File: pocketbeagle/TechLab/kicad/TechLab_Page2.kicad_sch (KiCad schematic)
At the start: 47 parts, among them T1 EAALSTIC1708A0, T2 3904, U5 MCP23S18-E/MJ, U6 FT230XQ-R, X2 10118192-0001LF

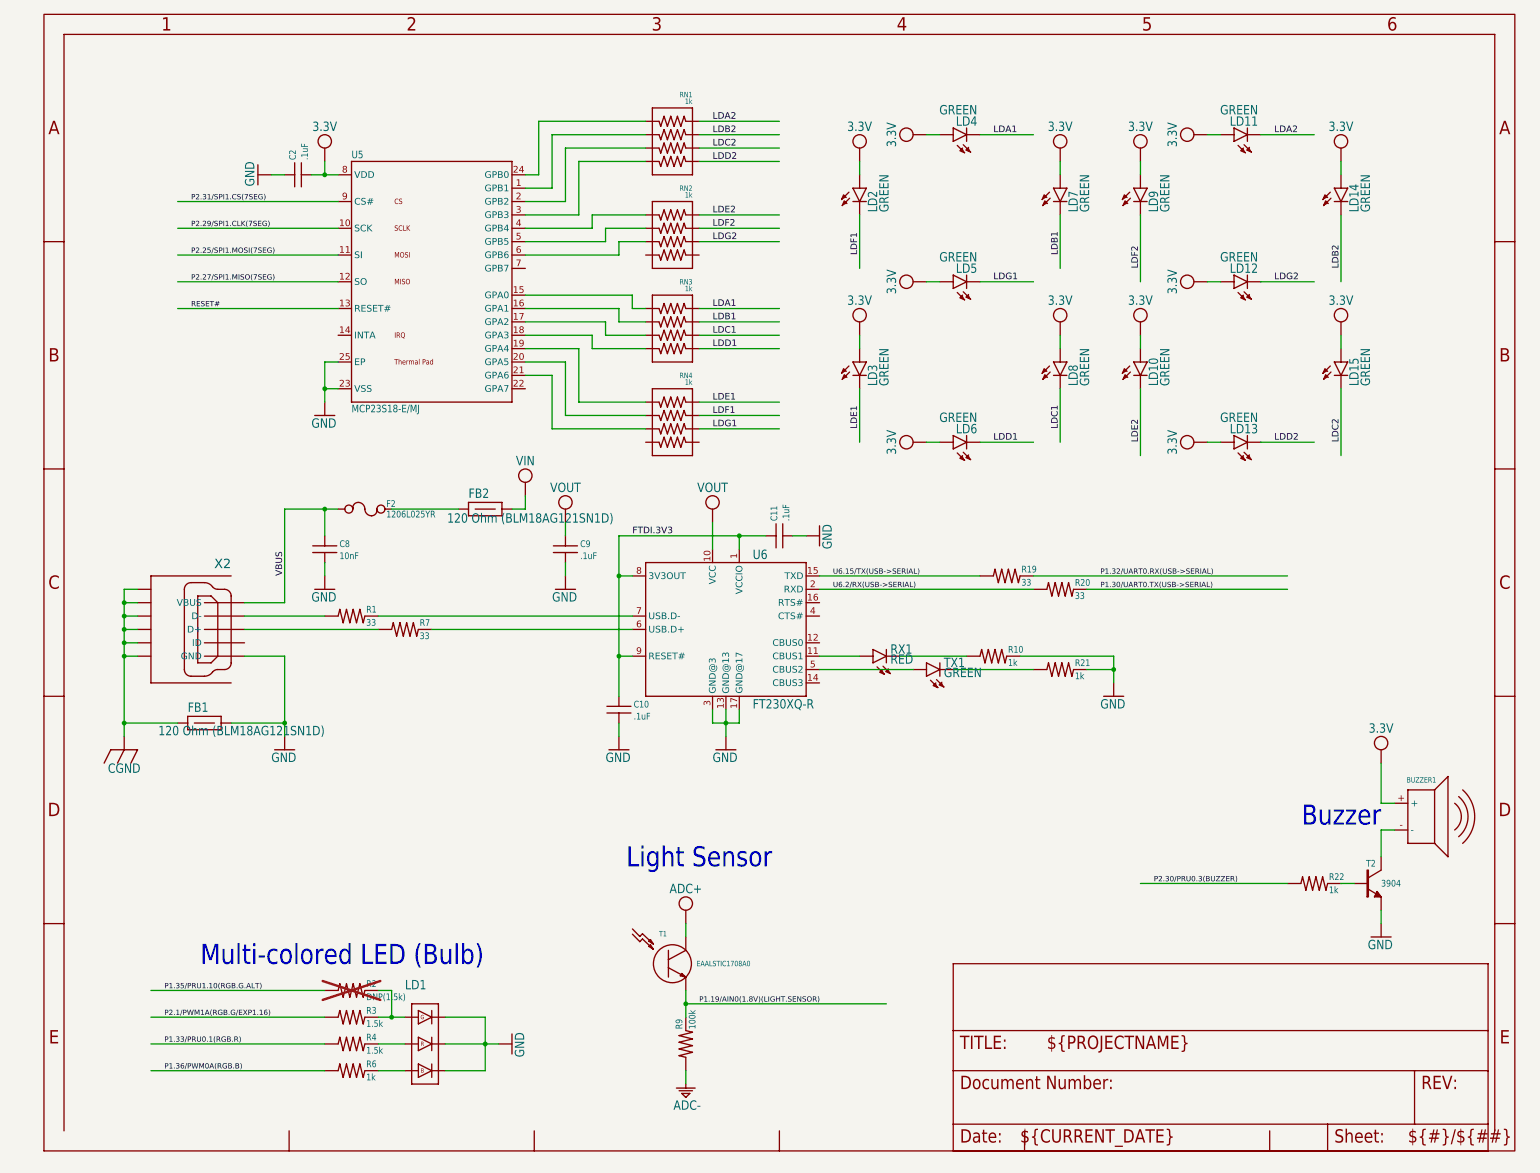
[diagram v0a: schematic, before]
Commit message: TechLab: Update title block for cleaner print
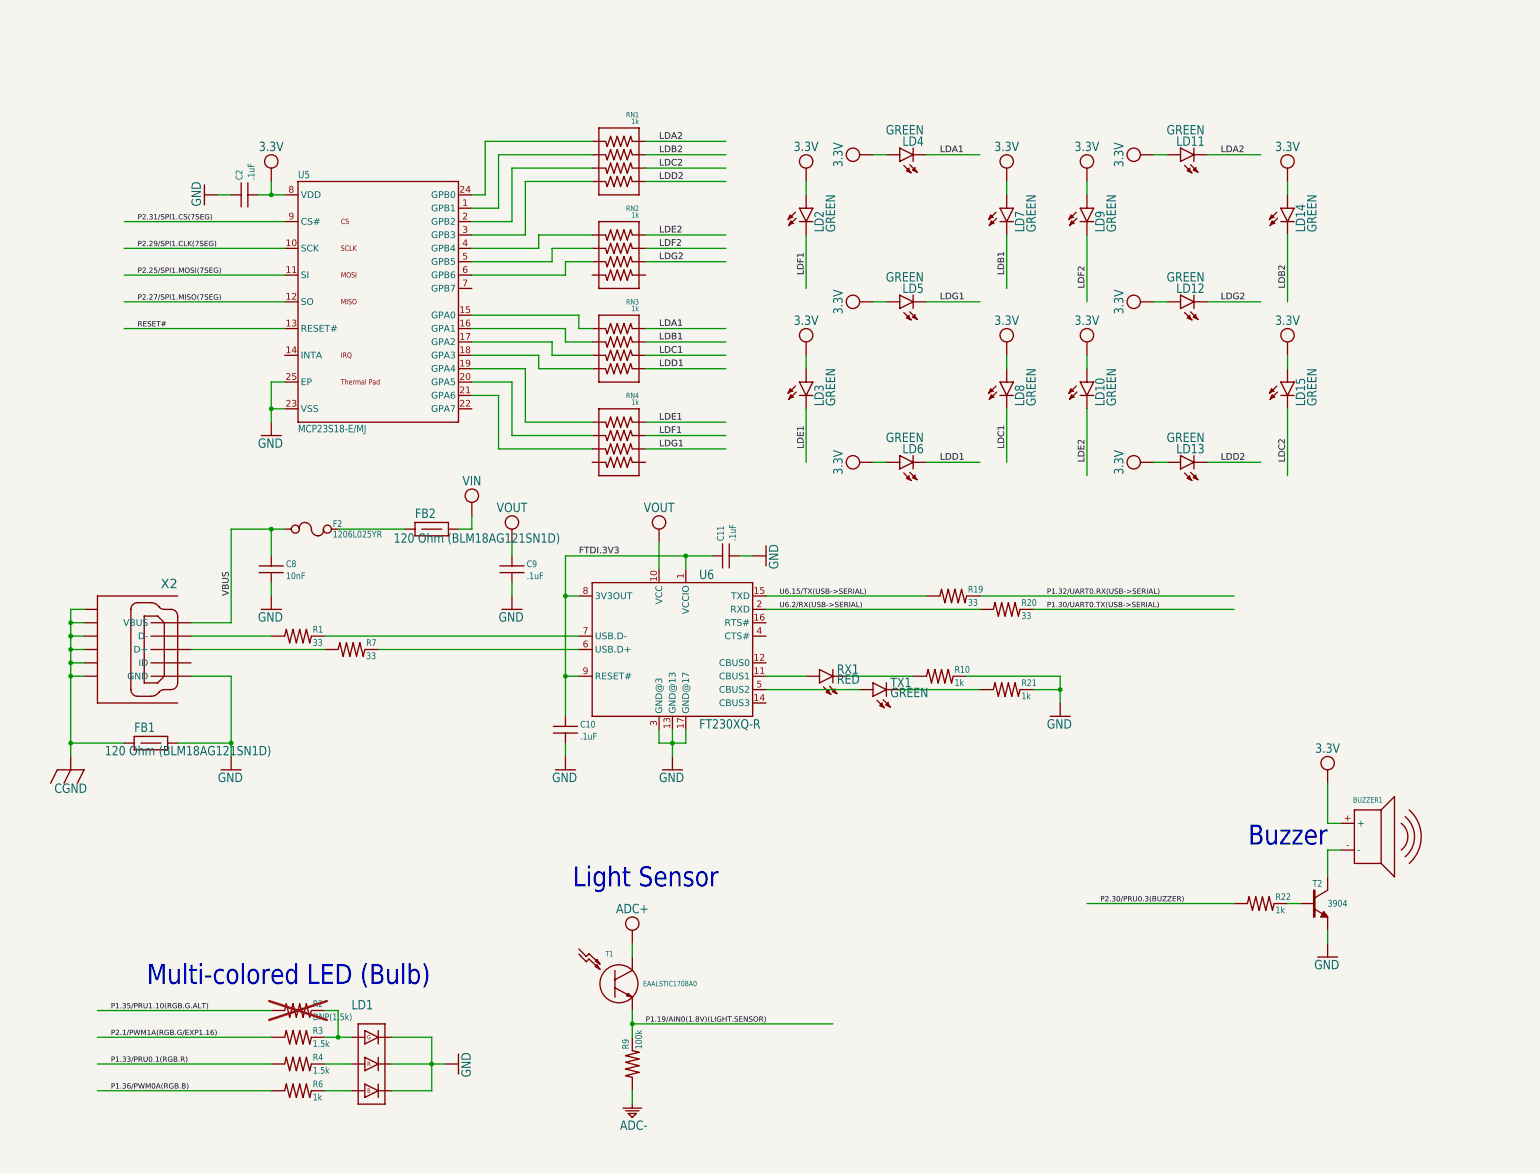
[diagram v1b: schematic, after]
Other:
- company: (none) -> BeagleBoard.org Foundation
- title: (none) -> PocketBeagle TechLab
- moved on the sheet: BUZZER1, C10, C11, C2, C8, C9, F2, FB1, FB2, LD1, LD10, LD11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

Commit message: Add USB C and 3-pin JST SH for UART with analog switch
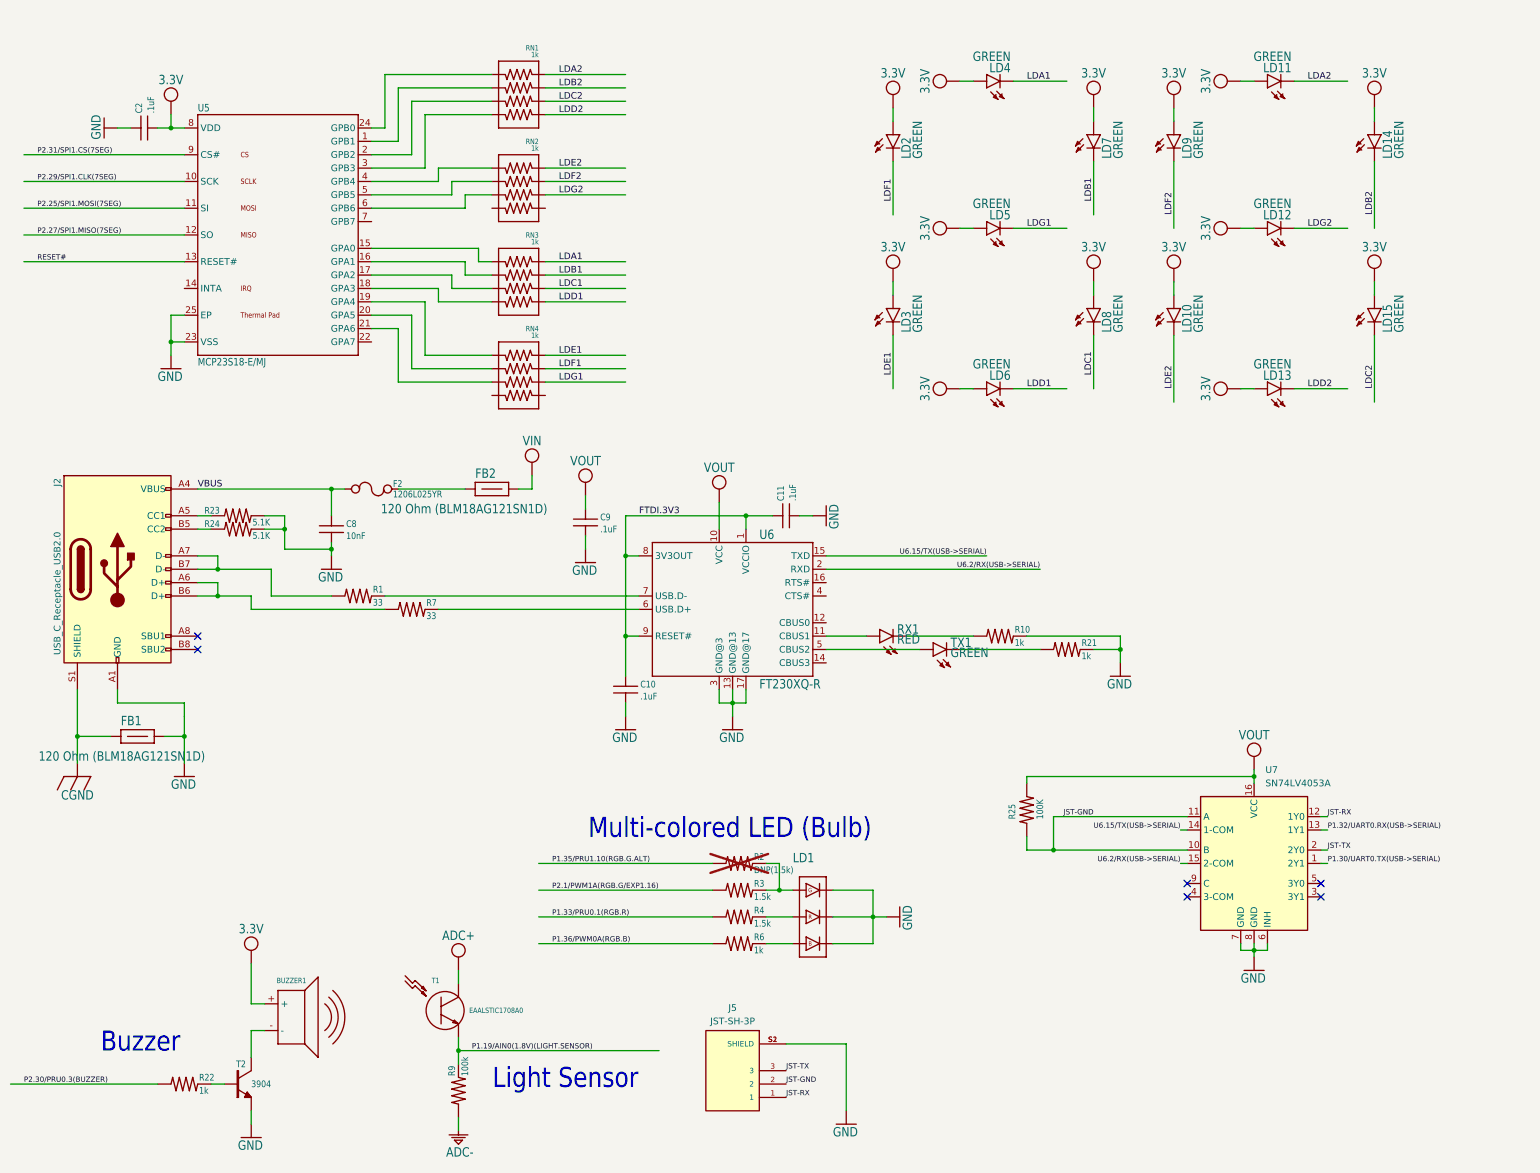
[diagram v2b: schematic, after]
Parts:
- removed R19, R20: 33, TechLab:0402, symbol TechLab-eagle-import:RESISTOR-(INCH)-0402
- removed X2: 10118192-0001LF, TechLab:10118192-0001LF(MICRO-USB-B-AMPHENOL-FCI), symbol TechLab-eagle-import:10118192-0001LF
- added J2: USB_C_Receptacle_USB2.0, Connector_USB:USB_C_Receptacle_GCT_USB4105-xx-A_16P_TopMnt_Horizontal, symbol Connector:USB_C_Receptacle_USB2.0
- added J5: JST-SH-3P, Upside Down Labs:JST-SH-3P, symbol Upside Down Labs:JST-SH-3P
- added R23, R24: 5.1K, Upside Down Labs:0402, symbol TechLab-eagle-import:RESISTOR-(INCH)-0402
- added R25: 100K, Upside Down Labs:0402, symbol TechLab-eagle-import:RESISTOR-(INCH)-0402
- added U7: SN74LV4053A, Upside Down Labs:SOT-23-THN-16, symbol Upside Down Labs:SN74LV4053A
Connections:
- net CGND: now also J2.S1 (SHIELD)
- net GND: now also J2.A1 (GND), J2.A12 (GND), J2.B1 (GND), J2.B12 (GND), J5.S1 (SHIELD), J5.S2 (SHIELD), R23.2, R24.2, U7.6 (INH), U7.7 (GND), U7.8 (GND)
- net P1.30/UART0.TX(USB->SERIAL): now also U7.1 (2Y1)
- net P1.32/UART0.RX(USB->SERIAL): now also U7.13 (1Y1)
- net U6.15/TX(USB->SERIAL): now also U7.14 (1-COM)
- net U6.2/RX(USB->SERIAL): now also U7.15 (2-COM)
- net VBUS: now also J2.A4 (VBUS), J2.A9 (VBUS), J2.B4 (VBUS), J2.B9 (VBUS)
- net VOUT: now also R25.2, U7.16 (VCC)
- net at R7.1: now also J2.A6 (D+), J2.B6 (D+)
- net at R1.1: now also J2.A7 (D-), J2.B7 (D-)
- new net: J2.A5 (CC1), R23.1
- new net: J2.B5 (CC2), R24.1
- new net JST-GND: J5.2, R25.1, U7.10 (B), U7.11 (A)
- new net JST-RX: J5.1, U7.12 (1Y0)
- new net JST-TX: J5.3, U7.2 (2Y0)
- no-connect marks 0 -> 6
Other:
- moved on the sheet: BUZZER1, C10, C11, C2, C8, C9, F2, FB1, FB2, LD1, LD10, LD11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

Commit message: TechLab: back-annotate BOM
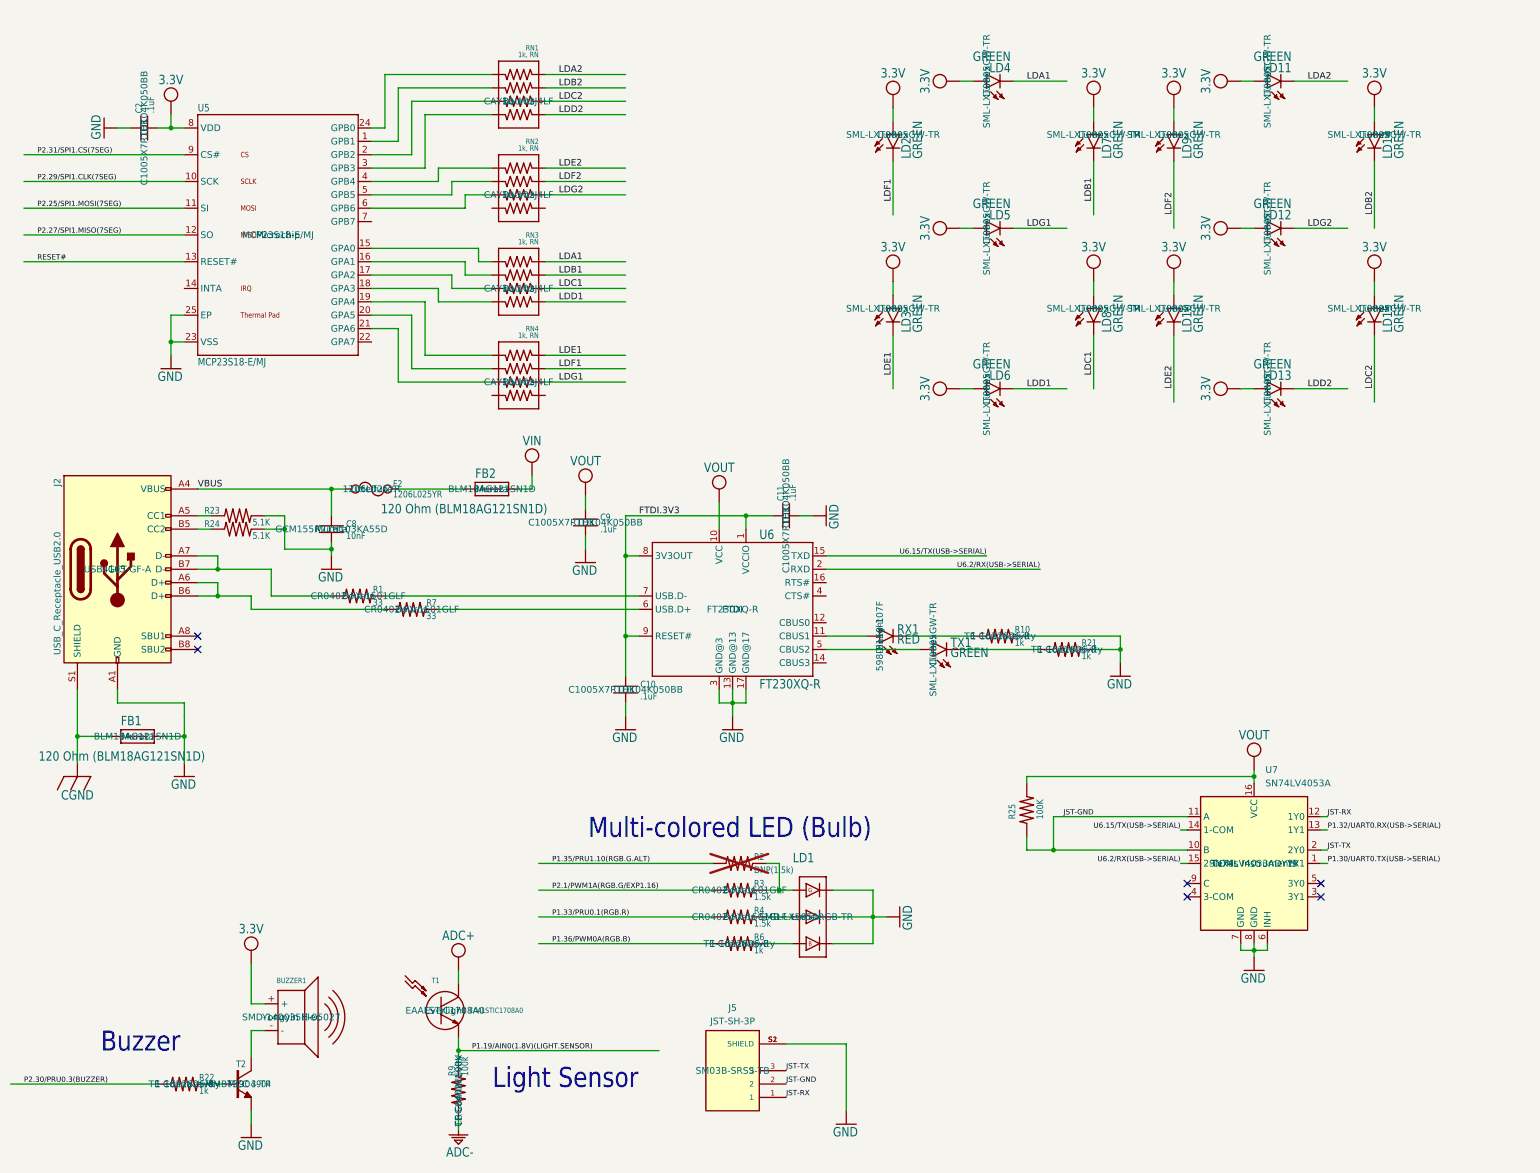
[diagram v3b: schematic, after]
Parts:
- BUZZER1: MANUFACTURER (none) -> Yongyin Elec; MPN (none) -> SMD-140035H-05027
- C10, C11, C2, C9: MANUFACTURER (none) -> TDK; MPN (none) -> C1005X7R1H104K050BB
- C8: MANUFACTURER (none) -> Murata; MPN (none) -> GCM155R71H103KA55D
- F2: MANUFACTURER (none) -> Littelfuse; MPN (none) -> 1206L025YR
- FB1, FB2: MANUFACTURER (none) -> Murata; MPN (none) -> BLM18AG121SN1D
- J2: MANUFACTURER (none) -> GCT; MPN (none) -> USB4105-GF-A
- J5: MPN (none) -> SM03B-SRSS-TB
- LD1: MANUFACTURER (none) -> Lumex; MPN (none) -> SMD-LX5050RGB-TR
- LD10, LD11, LD12, LD13, LD14, LD15, LD2, LD3, LD4, LD5, LD6, LD7, LD8, LD9, TX1: MANUFACTURER (none) -> Lumex; MPN (none) -> SML-LXT0805GW-TR
- R1, R3, R4, R7: MANUFACTURER (none) -> Bourns; MPN (none) -> CR0402-FX-1501GLF
- R10, R21, R22, R6: MANUFACTURER (none) -> TE Connectivity; MPN (none) -> 1-1622826-8
- R9: MANUFACTURER (none) -> TE Connectivity; MPN (none) -> CRG0402F100K
- RN1, RN2, RN3, RN4: value 1k -> 1k, RN; MANUFACTURER (none) -> Bourns; MPN (none) -> CAY10-102J4LF
- RX1: MANUFACTURER (none) -> Dialight; MPN (none) -> 598-8110-107F
- T1: MANUFACTURER (none) -> Everlight; MPN (none) -> EAALSTIC1708A0
- T2: MANUFACTURER (none) -> MCC; MPN (none) -> MMBT3904-TP
- U5: MANUFACTURER (none) -> Microchip; MPN (none) -> MCP23S18-E/MJ
- U6: MANUFACTURER (none) -> FTDI; MPN (none) -> FT230XQ-R
- U7: MANUFACTURER (none) -> Texas Instruments; MPN (none) -> SN74LV4053ADYYR
